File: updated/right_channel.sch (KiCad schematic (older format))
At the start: 24 parts, among them J4 Left 0 ohms, J5 Right 8 ohms, J6 Conn_Coaxial, T3 AudioTxfmr

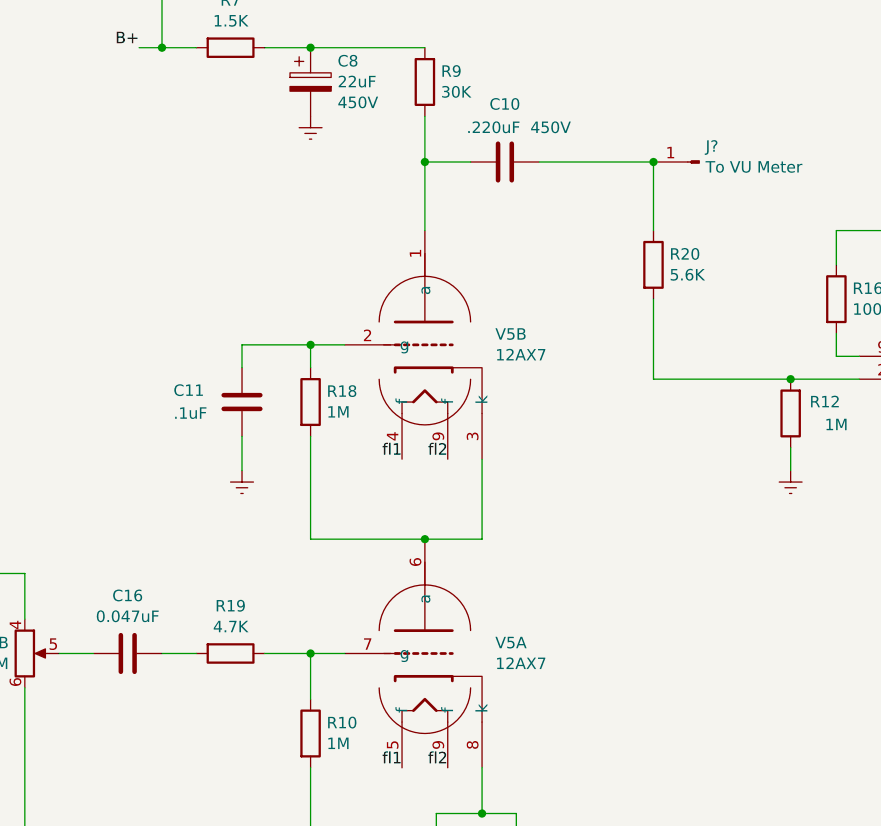
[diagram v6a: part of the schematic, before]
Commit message: remove grid stopped resistors.
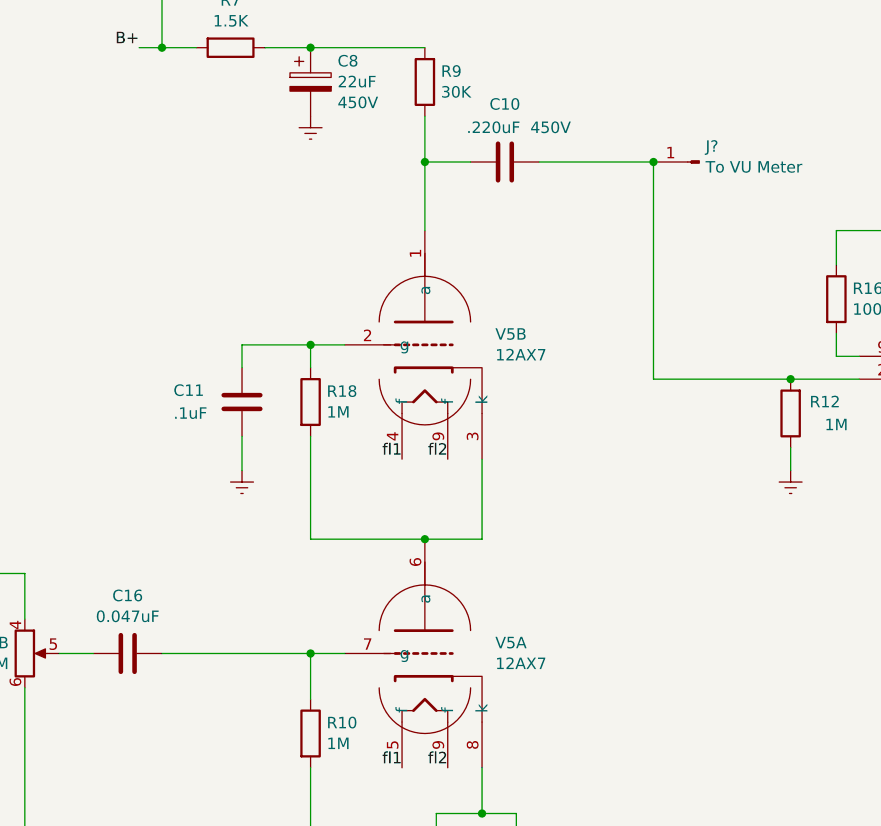
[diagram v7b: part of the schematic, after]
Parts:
- removed R19: 4.7K, symbol Device:R
- removed R20: 5.6K, symbol Device:R
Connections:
- net at C10.1, J?.1 (Pin_1): now also R12.2, V6.2 (g1)
- net at R10.1, V5.7 (g): now also C16.1
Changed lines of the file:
@@
 	3900 3550 3900 3400
-$Comp
-L Device:R R20
-U 1 1 5F56722A
-P 5700 2650
-F 0 "R20" H 5770 2696 50  0000 L CNN
-F 1 "5.6K" H 5770 2605 50  0000 L CNN
-F 2 "" V 5630 2650 50  0001 C CNN
-F 3 "~" H 5700 2650 50  0001 C CNN
-	1    5700 2650
-	1    0    0    -1
-$EndComp
-Wire Wire Line
-	5700 2500 5700 2200
-Wire Wire Line
-	5700 2800 5700 3150
 $Comp
 L Device:C C16
@@
 	0    1    1    0
 $EndComp
-$Comp
-L Device:R R19
-U 1 1 5F5828D1
-P 3850 4350
-F 0 "R19" V 3643 4350 50  0000 C CNN
-F 1 "4.7K" V 3734 4350 50  0000 C CNN
-F 2 "" V 3780 4350 50  0001 C CNN
-F 3 "~" H 3850 4350 50  0001 C CNN
-	1    3850 4350
-	0    1    1    0
-$EndComp
-Wire Wire Line
-	3550 4350 3700 4350
-Wire Wire Line
-	4000 4350 4200 4350
 Connection ~ 4200 4350
 Connection ~ 4200 5750
@@
 $EndComp
 Connection ~ 5700 2200
+Wire Wire Line
+	5700 2200 5700 3150
+Wire Wire Line
+	3550 4350 4200 4350
 $EndSCHEMATC

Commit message: update schematic
Replaced all the counterfeit capacitor between preamp and power stage. Really opened up the sound.
Add some pictures
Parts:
- removed C10: .220uF, Capacitor_THT:CP_Radial_D4.0mm_P2.00mm, symbol Device:C
- added C? (x2): 0.1uF, symbol Device:C
- C12, C8, C9: symbol Device:CP -> nobsound-audio-amplifier-rescue:CP-Device
- RV1: symbol Device:R_POT_Dual_Separate -> nobsound-audio-amplifier-rescue:R_POT_Dual_Separate-Device
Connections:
- net at R9.1, V5.1 (a): now also C?.2, C?.2
- net at J?.1 (Pin_1), R12.2, V6.2 (g1): now also C?.1, C?.1
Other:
- note added: "362V"
- note added: "364V"
- note added: "R = 2.2K\nV = 2.56V\nI = 1.16mA"
- note added: "R = 30.8K\nV = 35.3V\nI = 1.14mA"
- note added: "R = 460\nV = 15.72V\nI = 34.2mA\n"
- note added: "V = 355V"
- note added: "V = 9\nI = 34.2mA\nP = 308mW"
- note added: "Vplate = 355 - 15.72\nVplate = 339.3V\nI = 34.2mA\nP = 11.6W"
- note added: "Vplate = 362 - 35.3 - 2.66\nVplate = 324.04\nI = 1.1mA\nP = 356mW"
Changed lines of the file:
@@
 	6950 1950 6800 1950
 $Comp
-L Device:CP C?
+L nobsound-audio-amplifier-rescue:CP-Device C?
 U 1 1 5F20DF69
 P 4200 1850
@@
 $EndComp
 Connection ~ 4200 1700
-$Comp
-L Device:C C?
-U 1 1 5F20DF89
-P 5050 2200
-AR Path="/5F20DF89" Ref="C?"  Part="1"
-AR Path="/5F1F04D2/5F20DF89" Ref="C?"  Part="1"
-AR Path="/5F200EB9/5F20DF89" Ref="C10"  Part="1"
-F 0 "C10" V 4798 2200 50  0000 C CNN
-F 1 ".220uF" V 4900 2150 50  0000 C CNN
-F 2 "Capacitor_THT:CP_Radial_D4.0mm_P2.00mm" H 5088 2050 50  0001 C CNN
-F 3 "~" H 5050 2200 50  0001 C CNN
-F 4 "450V" V 4900 2400 50  0000 C CNN "Voltage"
-	1    5050 2200
-	0    1    1    0
-$EndComp
 Wire Wire Line
 	4900 2200 4700 2200
@@
 $EndComp
 $Comp
-L Device:CP C?
+L nobsound-audio-amplifier-rescue:CP-Device C?
 U 1 1 5F20DFD9
 P 5100 5350
@@
 	6950 2150 6950 2500
 $Comp
-L Device:CP C?
+L nobsound-audio-amplifier-rescue:CP-Device C?
 U 1 1 5F20E026
 P 7350 3950
@@
 	4700 3850 4950 3850
 $Comp
-L Device:R_POT_Dual_Separate RV1
+L nobsound-audio-amplifier-rescue:R_POT_Dual_Separate-Device RV1
 U 2 1 5F245DA2
 P 2950 4350
@@
 Connection ~ 4200 4350
 Connection ~ 4200 5750
+Wire Wire Line
+	5700 2200 5700 3150
+Wire Wire Line
+	3550 4350 4200 4350
+Connection ~ 5700 2200
 $Comp
 L Connector:Conn_01x01_Male J?
@@
 	-1   0    0    1
 $EndComp
-Connection ~ 5700 2200
-Wire Wire Line
-	5700 2200 5700 3150
-Wire Wire Line
-	3550 4350 4200 4350
+Text Notes 4500 1650 0    50   ~ 0
+362V
+Text Notes 3250 1600 0    50   ~ 0
+364V
+Text Notes 4200 2450 0    50   ~ 0
+R = 30.8K\nV = 35.3V\nI = 1.14mA
+Text Notes 4250 5500 0    50   ~ 0
+R = 2.2K\nV = 2.56V\nI = 1.16mA
+Text Notes 2750 3050 0    50   ~ 0
+Vplate = 362 - 35.3 - 2.66\nVplate = 324.04\nI = 1.1mA\nP = 356mW
+Text Notes 7850 3950 0    50   ~ 0
+R = 460\nV = 15.72V\nI = 34.2mA\n
+Text Notes 7650 3200 0    50   ~ 0
+Vplate = 355 - 15.72\nVplate = 339.3V\nI = 34.2mA\nP = 11.6W
+Text Notes 7100 2550 0    50   ~ 0
+V = 355V
+Text Notes 7550 1500 0    50   ~ 0
+V = 9\nI = 34.2mA\nP = 308mW
+$Comp
+L Device:C C?
+U 1 1 5F858C56
+P 5050 2100
+F 0 "C?" V 4798 2100 50  0000 C CNN
+F 1 "0.1uF" V 4889 2100 50  0000 C CNN
+F 2 "" H 5088 1950 50  0001 C CNN
+F 3 "~" H 5050 2100 50  0001 C CNN
+	1    5050 2100
+	0    1    1    0
+$EndComp
+$Comp
+L Device:C C?
+U 1 1 5F858C5C
+P 5050 2300
+F 0 "C?" V 5200 2200 50  0000 C CNN
+F 1 "0.1uF" V 5300 2200 50  0000 C CNN
+F 2 "" H 5088 2150 50  0001 C CNN
+F 3 "~" H 5050 2300 50  0001 C CNN
+	1    5050 2300
+	0    1    1    0
+$EndComp
+Wire Wire Line
+	5200 2100 5200 2200
+Wire Wire Line
+	5200 2200 5200 2300
+Connection ~ 5200 2200
+Wire Wire Line
+	4900 2100 4900 2200
+Wire Wire Line
+	4900 2200 4900 2300
+Connection ~ 4900 2200
 $EndSCHEMATC
